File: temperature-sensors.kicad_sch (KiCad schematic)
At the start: 14 parts, among them SW1 SW_Push, U1 nRF52840-QFXX, Y1 32MHz, Y2 32.768kHz

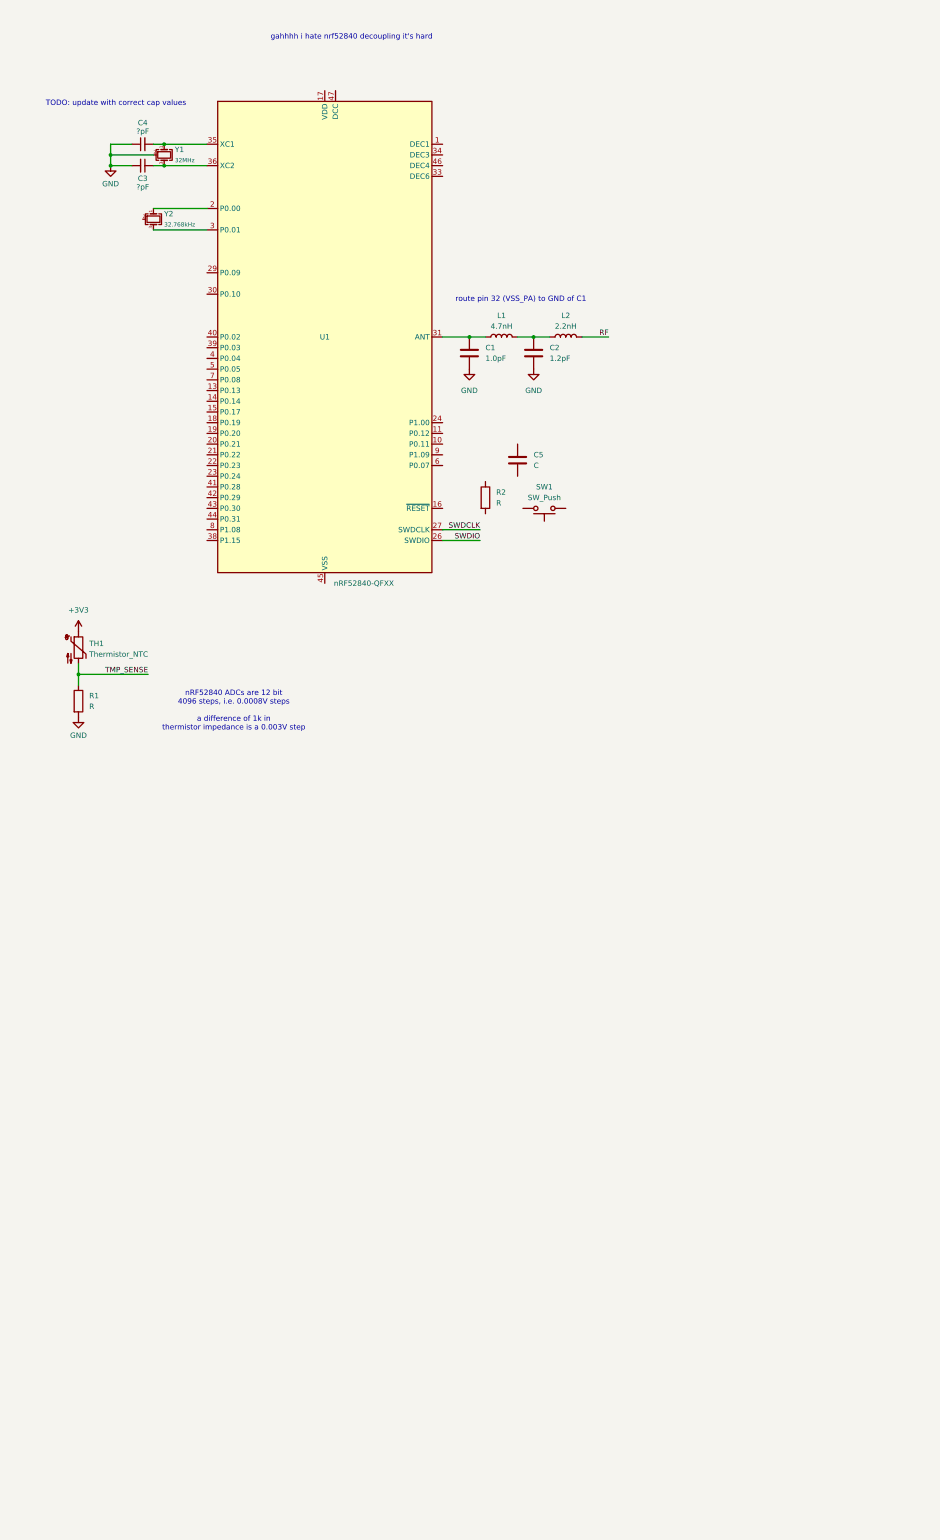
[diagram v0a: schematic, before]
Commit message: add actually decent power circuitry - can charge and power itself off USB simultaneously
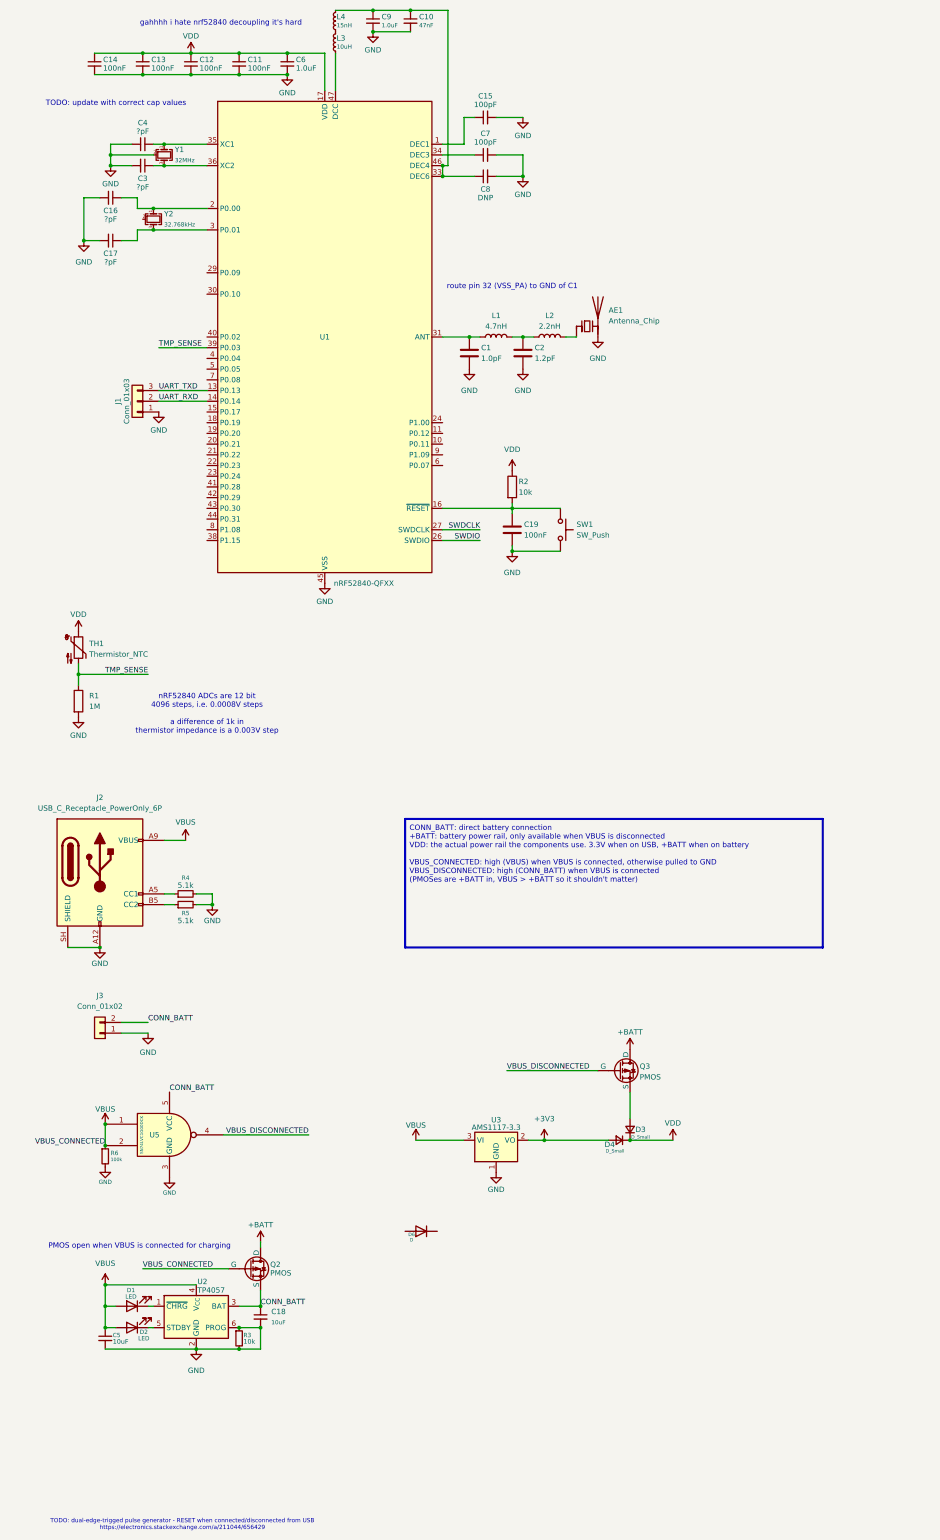
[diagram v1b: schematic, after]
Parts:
- removed C5: C, symbol KiCad:C
- added AE1: Antenna_Chip, symbol KiCad:Antenna_Chip
- added C10: 47nF, symbol KiCad:C_Small
- added C11, C12, C13, C14: 100nF, symbol KiCad:C_Small
- added C15, C7: 100pF, symbol KiCad:C_Small
- added C16, C17: ?pF, symbol KiCad:C_Small
- added C18, C5: 10uF, symbol KiCad:C_Small
- added C19: 100nF, symbol KiCad:C
- added C6, C9: 1.0uF, symbol KiCad:C_Small
- added C8: DNP, symbol KiCad:C_Small
- added D1, D2: LED, symbol KiCad:LED
- added D3, D4: D_Small, symbol KiCad:D_Small
- added D6: D, symbol KiCad:D
- added J1: Conn_01x03, symbol KiCad:Conn_01x03
- added J2: USB_C_Receptacle_PowerOnly_6P, symbol KiCad:USB_C_Receptacle_PowerOnly_6P
- added J3: Conn_01x02, symbol KiCad:Conn_01x02
- added L3: 10uH, symbol KiCad:L_Small
- added L4: 15nH, symbol KiCad:L_Small
- added Q2, Q3: PMOS, symbol KiCad:PMOS
- added R3: 10k, symbol KiCad:R_Small
- added R4, R5: 5.1k, symbol KiCad:R_Small
- added R6: 100k, symbol KiCad:R_Small
- added U2: TP4057, Package_TO_SOT_SMD:TSOT-23-6, symbol KiCad:TP4057
- added U3: AMS1117-3.3, Package_TO_SOT_SMD:SOT-223-3_TabPin2, symbol KiCad:AMS1117-3.3
- added U5: SN74LVC1G00DCK, Package_TO_SOT_SMD:Texas_R-PDSO-G5_DCK-5, symbol KiCad:SN74LVC1G00DCK
- R1: value R -> 1M
- R2: value R -> 10k
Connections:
- net +3V3: now also D4.2 (A), U3.2 (VO); no longer TH1.1
- net GND: now also SW1.2, U1.32 (VSS_PA), U1.45 (VSS), U1.49 (VSS), AE1.2 (PCB_Trace), C10.2, C11.2, C12.2, C13.2, C14.2, C15.2, C16.2, C17.2, C18.2, C19.2, C5.2, C6.2, C7.2, C8.2, C9.2, J1.1 (Pin_1), J2.A12 (GND), J2.B12 (GND), J2.SH (SHIELD), J3.1 (Pin_1), R3.1, R3.2, R4.2, R5.2, R6.2, U2.2 (GND), U2.6 (PROG), U3.1 (GND), U5.3 (GND)
- net TMP_SENSE: now also U1.39 (P0.03)
- net at U1.2 (P0.00), Y2.1: now also C16.1
- net at U1.3 (P0.01), Y2.3: now also C17.1
- net at SW1.1: now also R2.2, U1.16 (~{RESET}), C19.1
- net VDD: now reaches R2.1
- net VDD: now also TH1.1, U1.12 (VDD), U1.17 (VDD), U1.25 (VDD), U1.37 (VDD), U1.48 (VDD), C11.1, C12.1, C13.1, C14.1, C6.1, D3.1 (K), D4.1 (K)
- net at U1.1 (DEC1): now also C15.1
- net UART_TXD: now reaches U1.13 (P0.13)
- net UART_TXD: now also J1.3 (Pin_3)
- net UART_RXD: now reaches U1.14 (P0.14)
- net UART_RXD: now also J1.2 (Pin_2)
- net at U1.33 (DEC6): now also U1.46 (DEC4), C10.1, C8.1, C9.1, L4.2
- net at U1.34 (DEC3): now also C7.1
- net at U1.47 (DCC): now also L3.1
- net RF: no longer names the net of L2.2
- net RF: now also AE1.1 (FEED)
- new net: J2.A5 (CC1), R4.1
- new net: D3.2 (A), Q3.3 (S)
- new net: L3.2, L4.1
- new net: D2.1 (K), U2.5 (STDBY)
- new net: J2.B5 (CC2), R5.1
- new net: D1.1 (K), U2.1 (~{CHRG})
- new net +BATT: Q2.1 (D), Q3.1 (D)
- new net CONN_BATT: C18.1, J3.2 (Pin_2), Q2.3 (S), U2.3 (BAT), U5.5 (VCC)
- new net VBUS: C5.1, D1.2 (A), D2.2 (A), J2.A9 (VBUS), J2.B9 (VBUS), Q2.2 (G), R6.1, U2.4 (V_{CC}), U3.3 (VI), U5.1, U5.2
- new net VBUS_DISCONNECTED: Q3.2 (G), U5.4
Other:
- note added: "CONN_BATT: direct battery connection +BATT: battery power rail, only available when VBUS is disconnected VDD: the actual power rail the components use. 3.3V when on USB, +BATT when on battery VBUS_CONNECTED: high (VBUS) when VBUS is connected, otherwise pulled to GND VBUS_DISCONNECTED: high (CONN_BATT) when VBUS is connected (PMOSes are +BATT in, VBUS > +BATT so it shouldn't matter)"
- note added: "PMOS open when VBUS is connected for charging"
- note added: "TODO: dual-edge-trigged pulse generator - RESET when connected/disconnected from USB https://electronics.stackexchange.com/a/211044/656429"
- moved on the sheet: C2, L1, L2

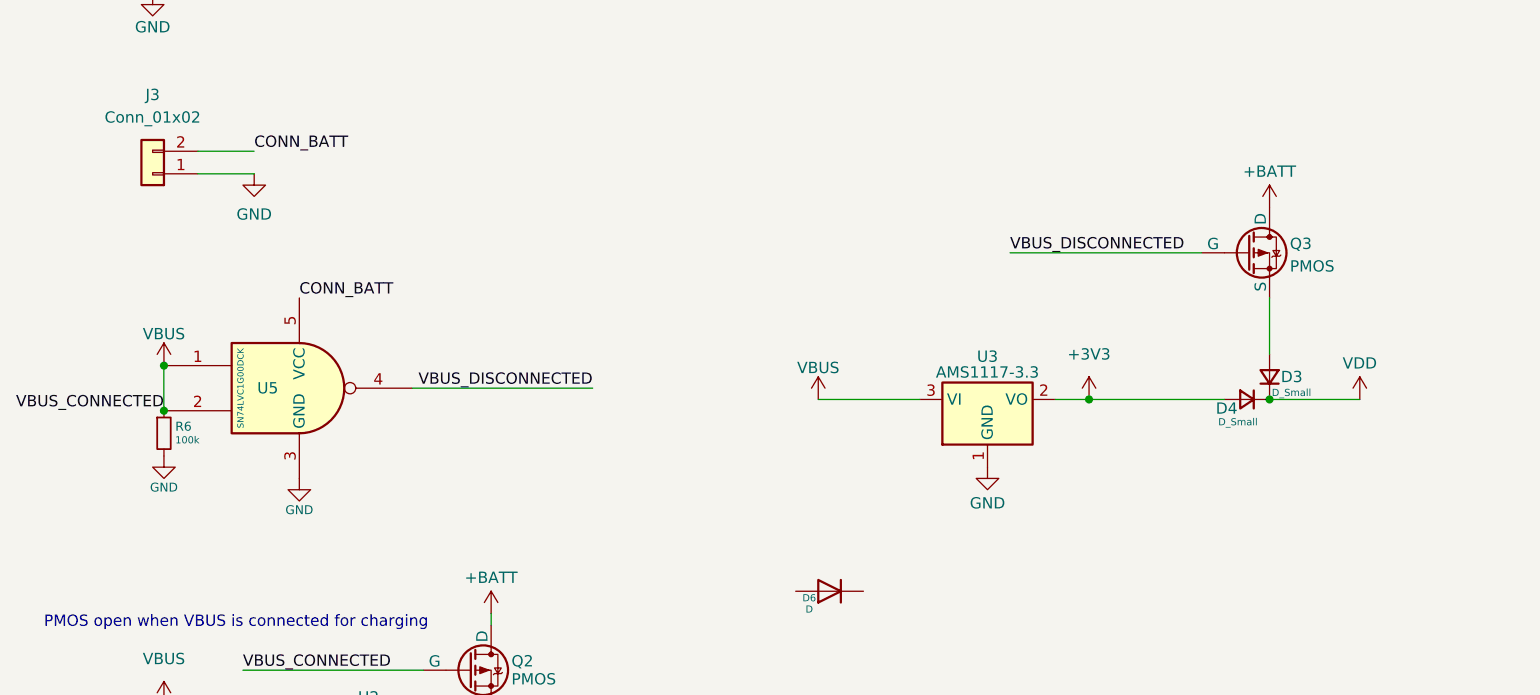
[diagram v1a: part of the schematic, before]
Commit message: get rid of extra PMOS
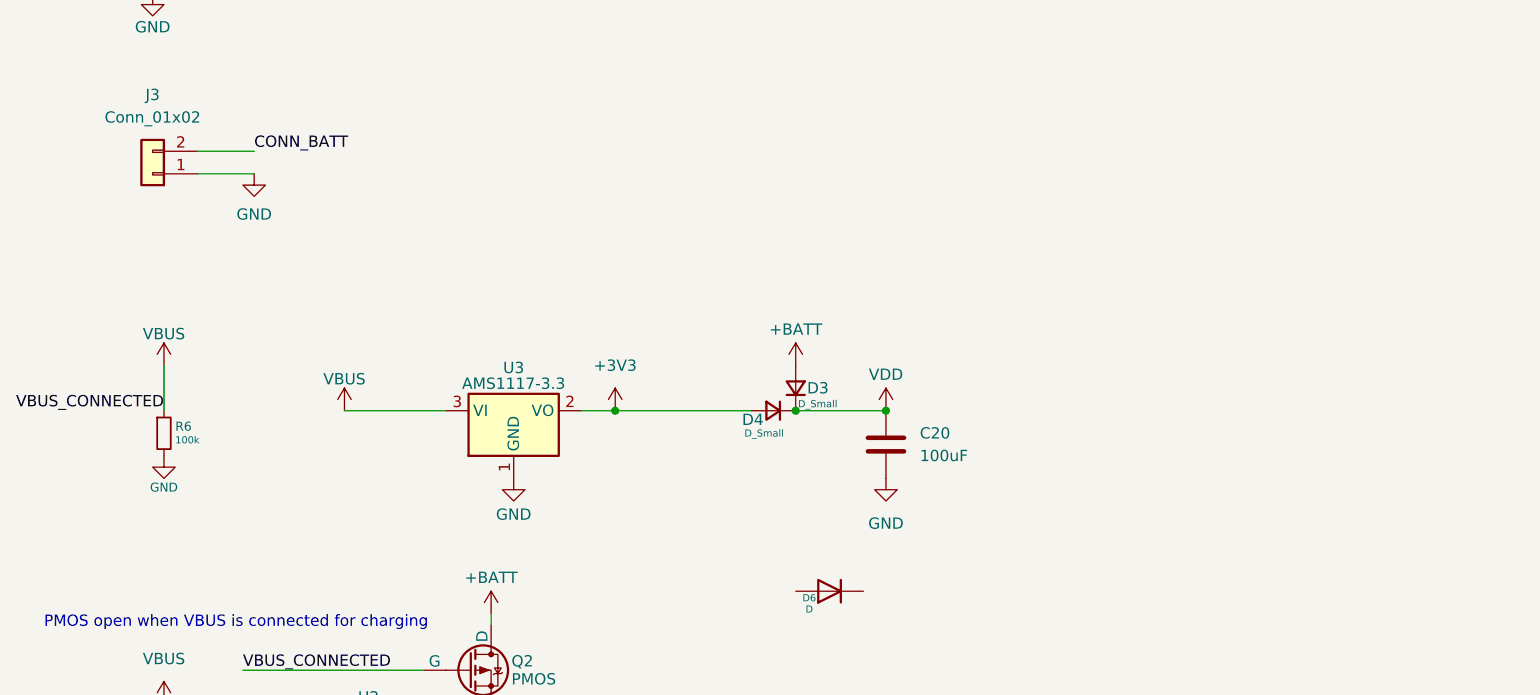
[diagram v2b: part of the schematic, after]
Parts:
- removed Q3: PMOS, symbol KiCad:PMOS
- removed U5: SN74LVC1G00DCK, Package_TO_SOT_SMD:Texas_R-PDSO-G5_DCK-5, symbol KiCad:SN74LVC1G00DCK
- added C20: 100uF, symbol KiCad:C
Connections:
- net +BATT: now also D3.2 (A)
- net GND: now also C20.2
- net VDD: now also C20.1
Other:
- moved on the sheet: D3, D4, U3

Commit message: add a bunch of stuff idk i'm just committing
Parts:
- added D7: D, symbol KiCad:D
- added J4: Conn_01x04, symbol KiCad:Conn_01x04
- added Q3, Q4: PMOS, symbol KiCad:PMOS
- added R7: 100k, symbol KiCad:R_Small
- added SW2: SW_SPST, symbol KiCad:SW_SPST
- added U5: SN74LVC1G00DCK, Package_TO_SOT_SMD:Texas_R-PDSO-G5_DCK-5, symbol KiCad:SN74LVC1G00DCK
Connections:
- net +BATT: now also D6.2 (A), Q3.1 (D); no longer D3.2 (A)
- net CONN_BATT: now also SW2.2 (B), U5.5 (VCC)
- net GND: now also J4.1 (Pin_1), R7.2, U5.3 (GND)
- net SWDCLK: now also J4.3 (Pin_3)
- net SWDIO: now also J4.4 (Pin_4)
- net VBUS: now also D7.2 (A); no longer U3.3 (VI)
- net at D6.1 (K): now also Q4.1 (D)
- net RESET: now reaches C19.1, R2.2, SW1.1, U1.16 (~{RESET})
- net RESET: now also J4.2 (Pin_2)
- new net: D7.1 (K), Q4.3 (S), U3.3 (VI)
- new net: D3.2 (A), Q3.3 (S)
- new net DISABLE_3V3_ON_BATT: Q3.2 (G), U5.4
- new net ENABLE_3V3_ON_BATT: Q4.2 (G), R7.1, SW2.1 (A), U5.1, U5.2
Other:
- note added: "CONN_BATT: direct battery connection +BATT: battery power rail, only available when VBUS is disconnected VDD: the actual power rail the components use. 3.3V when on USB, +BATT when on battery VBUS_CONNECTED: high (VBUS) when VBUS is connected, otherwise pulled to GND (PMOSes are +BATT in, VBUS > +BATT so it shouldn't matter) ENABLE_3V3_ON_BATT: high (CONN_BATT) when 3.3V on BATT is enabled, other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"
- note added: "VBUS is handled by the PMOS near charging, so don't need to worry about that here"
- note removed: "CONN_BATT: direct battery connection +BATT: battery power rail, only available when VBUS is disconnected VDD: the actual power rail the components use. 3.3V when on USB, +BATT when on battery VBUS_CONNECTED: high (VBUS) when VBUS is connected, otherwise pulled to GND VBUS_DISCONNECTED: high (CONN_BATT) when VBUS is connected (PMOSes are +BATT in, VBUS > +BATT so it shouldn't matter)"
- moved on the sheet: C20, D3, D4, D6, R6, U3

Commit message: finished schematic idk
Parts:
- removed Q2, Q3, Q4: PMOS, symbol KiCad:PMOS
- added Q1, Q2, Q3: AO3401A, Package_TO_SOT_SMD:SOT-23, symbol Transistor_FET:AO3401A
- added R8, R9: 300, Resistor_SMD:R_0603_1608Metric, symbol Device:R_Small
- added TH2: Thermistor_NTC, Resistor_SMD:R_0402_1005Metric, symbol KiCad:Thermistor_NTC
- added TH3: Thermistor_NTC, Resistor_SMD:R_0603_1608Metric, symbol KiCad:Thermistor_NTC
- added TH4: Thermistor_NTC, Resistor_SMD:R_0805_2012Metric, symbol KiCad:Thermistor_NTC
- AE1: footprint (none) -> RF_Antenna:Johanson_2450AT43F0100
- C1, C10, C11, C12, C13, C14, C15, C16, C17, C18, C19, C2, C20, C3, C4, C5, C6, C7, C8, C9: footprint (none) -> Capacitor_SMD:C_0603_1608Metric
- D1, D2: footprint (none) -> Diode_SMD:D_0603_1608Metric
- D3, D4, D6, D7: footprint (none) -> Diode_SMD:D_SOD-323
- J1: footprint (none) -> Connector_JST:JST_PH_S3B-PH-SM4-TB_1x03-1MP_P2.00mm_Horizontal
- J2: footprint (none) -> Connector_USB:USB_C_Receptacle_GCT_USB4135-GF-A_6P_TopMnt_Horizontal
- J3: footprint (none) -> Connector_JST:JST_PH_S2B-PH-SM4-TB_1x02-1MP_P2.00mm_Horizontal
- J4: footprint (none) -> Connector_JST:JST_PH_S4B-PH-SM4-TB_1x04-1MP_P2.00mm_Horizontal
- L1, L2, L4: footprint (none) -> Inductor_SMD:L_0402_1005Metric
- L3: footprint (none) -> Inductor_SMD:L_0603_1608Metric
- R1, R2, R3, R4, R5, R6, R7: footprint (none) -> Resistor_SMD:R_0603_1608Metric
- SW1: footprint (none) -> Button_Switch_SMD:SW_SPST_TS-1088-xR020
- SW2: footprint (none) -> Button_Switch_SMD:SW_DIP_SPSTx01_Slide_Copal_CHS-01B_W7.62mm_P1.27mm
- TH1: footprint (none) -> Resistor_SMD:R_0201_0603Metric
- Y1, Y2: footprint (none) -> Crystal:Crystal_SMD_3225-4Pin_3.2x2.5mm
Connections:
- net +BATT: now also Q1.3 (D), Q2.3 (D)
- net CONN_BATT: now also Q1.2 (S)
- net DISABLE_3V3_ON_BATT: now also Q2.1 (G)
- net ENABLE_3V3_ON_BATT: now also Q3.1 (G)
- net GND: now also C16.1, Y2.2 (G), Y2.4 (G); no longer C16.2
- net TMP_SENSE: now also TH2.2, TH3.2, TH4.2
- net VBUS: now also Q1.1 (G)
- net VDD: now also TH2.1, TH3.1, TH4.1
- net at D6.1 (K): now also Q3.3 (D)
- net at D7.1 (K), U3.3 (VI): now also Q3.2 (S)
- net at D3.2 (A): now also Q2.2 (S)
- net at U1.2 (P0.00), Y2.1: now also C16.2; no longer C16.1
- net at D2.1 (K): now also R8.1; no longer U2.5 (STDBY)
- net at D1.1 (K): now also R9.1; no longer U2.1 (~{CHRG})
- new net: R9.2, U2.1 (~{CHRG})
- new net: R8.2, U2.5 (STDBY)
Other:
- note added: "VBUS is handled by the PMOS near charging circuitry, so don't need to worry about that here"
- note removed: "VBUS is handled by the PMOS near charging, so don't need to worry about that here"
- moved on the sheet: C3, C4, C5, D1, D2, Y1

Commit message: aaaaaa
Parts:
- removed U3: AMS1117-3.3, Package_TO_SOT_SMD:SOT-223-3_TabPin2, symbol KiCad:AMS1117-3.3
- added L5: 1.5uH, symbol KiCad:L_Small
- added U3: (no value), temp-sensors:TPS63051-QFN-12-HotRod, symbol temp-sensors:TPS63051
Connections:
- net GND: now also U3.2 (GND)
- net at D7.1 (K), Q3.2 (S): now also U3.10 (I_{LIM}0), U3.11 (EN), U3.12 (V_{IN})
- new net: L5.1, U3.1 (L1)
- new net: L5.2, U3.3 (L2)
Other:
- moved on the sheet: C20, D3, D4, D7, Q2

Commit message: the pcb is pcb'd idkkkk
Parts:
- removed J4: Conn_01x04, Connector_JST:JST_PH_S4B-PH-SM4-TB_1x04-1MP_P2.00mm_Horizontal, symbol KiCad:Conn_01x04
- added C21: 1nF, Capacitor_SMD:C_0603_1608Metric, symbol Device:C_Small
- added C22: 10pF, Capacitor_SMD:C_0603_1608Metric, symbol Device:C_Small
- added C23: 10uF, Capacitor_SMD:C_0603_1608Metric, symbol KiCad:C
- added H1, H2, H3: MountingHole, MountingHole:MountingHole_2.2mm_M2_ISO7380, symbol Mechanical:MountingHole
- added J4: Conn_01x03, Connector_JST:JST_PH_S3B-PH-SM4-TB_1x03-1MP_P2.00mm_Horizontal, symbol Connector_Generic:Conn_01x03
- added R10: 560k, Resistor_SMD:R_0603_1608Metric, symbol Device:R_Small
- added R11: 180k, Resistor_SMD:R_0603_1608Metric, symbol Device:R_Small
- added R12: 1M, Resistor_SMD:R_0603_1608Metric, symbol Device:R_Small
- L5: footprint (none) -> Inductor_SMD:L_1008_2520Metric
- R7: value 100k -> 1M
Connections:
- net +3V3: now also U3.4 (V_{OUT}), C23.1, R10.1
- net GND: now also U3.6 (PFM/PWM), U3.[2,9] (GND), C21.2, C22.2, C23.2, J4.1 (Pin_1), R11.2; no longer R3.1, U2.6 (PROG), U3.2 (GND)
- net SWDCLK: now also J4.2 (Pin_2)
- net SWDIO: now also J4.3 (Pin_3)
- net 32M+: now reaches C4.2, U1.35 (XC1), Y1.1
- net 32768-: now reaches C17.1, U1.3 (P0.01), Y2.3
- net 32M-: now reaches C3.1, U1.36 (XC2), Y1.3
- net 32768+: now reaches C16.2, U1.2 (P0.00), Y2.1
- net at D7.1 (K), Q3.2 (S), U3.10 (I_{LIM}0)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: now also R12.1
- net at U3.5 (FB): now also C22.1, R10.2, R11.1
- net at U3.7 (SS): now also C21.1
- net at U3.8 (PG): now also R12.2
- new net: R3.1, U2.6 (PROG)
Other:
- moved on the sheet: C20, D3, D4, Q2

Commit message: add BOM and images and yeag
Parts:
- C16, C17: value ?pF -> 15pF
- C20: footprint Capacitor_SMD:C_0603_1608Metric -> Capacitor_SMD:C_0805_2012Metric
- C3, C4: value ?pF -> 20pF
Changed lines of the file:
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@@
 			)
 		)
-		(property "Value" "?pF"
+		(property "Value" "20pF"
 			(at 46.99 51.562 90)
 			(show_name no)
@@
 			)
 		)
-		(property "Value" "?pF"
+		(property "Value" "15pF"
 			(at 40.64 80.01 90)
 			(show_name no)
@@
 			)
 		)
-		(property "Footprint" "Capacitor_SMD:C_0603_1608Metric"
+		(property "Footprint" "Capacitor_SMD:C_0805_2012Metric"
 			(at 209.2452 302.26 0)
 			(hide yes)
@@
 			)
 		)
-		(property "Value" "?pF"
+		(property "Value" "20pF"
 			(at 46.99 64.77 90)
 			(show_name no)
@@
 			)
 		)
-		(property "Value" "?pF"
+		(property "Value" "15pF"
 			(at 40.64 66.802 90)
 			(show_name no)
